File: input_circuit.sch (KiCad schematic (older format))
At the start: 10 parts, among them J2 IN, U3 MCP6004

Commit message: Layout complete
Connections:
- net OUT: now also U3.14; no longer U3.1
- net Vref: now also U3.13 (-); no longer U3.2 (-)
- net at C12.1, D4.2 (A), R5.2: now also U3.12 (+); no longer U3.3 (+)
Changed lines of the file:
@@
 AR Path="/5AD35DB7/5AD30D7B/5AD2255F" Ref="D33"  Part="1"
 AR Path="/5AD35DB7/5AD30D85/5AD2255F" Ref="D35"  Part="1"
-F 0 "D4" H 3200 2230 50  0000 L CNN
+F 0 "D18" H 3200 2230 50  0000 L CNN
 F 1 "4142" H 3100 2070 50  0000 L CNN
 F 2 "Diodes_SMD:D_MiniMELF_Standard" V 3250 2150 50  0001 C CNN
@@
 AR Path="/5AD35DB7/5AD30D7B/5AD22566" Ref="R46"  Part="1"
 AR Path="/5AD35DB7/5AD30D85/5AD22566" Ref="R49"  Part="1"
-F 0 "R4" H 2280 2370 50  0000 L CNN
+F 0 "R25" H 2280 2370 50  0000 L CNN
 F 1 "22k" H 2280 2310 50  0000 L CNN
 F 2 "Resistors_SMD:R_0603_HandSoldering" H 2250 2350 50  0001 C CNN
@@
 AR Path="/5AD35DB7/5AD30D7B/5AD2256D" Ref="C43"  Part="1"
 AR Path="/5AD35DB7/5AD30D85/5AD2256D" Ref="C45"  Part="1"
-F 0 "C12" H 3260 2620 50  0000 L CNN
+F 0 "C26" H 3260 2620 50  0000 L CNN
 F 1 "47n" H 3260 2470 50  0000 L CNN
 F 2 "Capacitors_SMD:C_0603_HandSoldering" H 3250 2550 50  0001 C CNN
@@
 AR Path="/5AD222D9/5AD22574" Ref="#PWR?"  Part="1"
 AR Path="/5AD2476B/5AD22574" Ref="#PWR?"  Part="1"
-AR Path="/5AD2F8CE/5AD30D3F/5AD22574" Ref="#PWR020"  Part="1"
-AR Path="/5AD2F8CE/5AD30D49/5AD22574" Ref="#PWR023"  Part="1"
-AR Path="/5AD2F8CE/5AD30D53/5AD22574" Ref="#PWR026"  Part="1"
-AR Path="/5AD2F8CE/5AD30D5D/5AD22574" Ref="#PWR029"  Part="1"
-AR Path="/5AD2F8CE/5AD30D67/5AD22574" Ref="#PWR032"  Part="1"
-AR Path="/5AD2F8CE/5AD30D71/5AD22574" Ref="#PWR035"  Part="1"
-AR Path="/5AD2F8CE/5AD30D7B/5AD22574" Ref="#PWR038"  Part="1"
-AR Path="/5AD2F8CE/5AD30D85/5AD22574" Ref="#PWR041"  Part="1"
+AR Path="/5AD2F8CE/5AD30D3F/5AD22574" Ref="#PWR24"  Part="1"
+AR Path="/5AD2F8CE/5AD30D49/5AD22574" Ref="#PWR27"  Part="1"
+AR Path="/5AD2F8CE/5AD30D53/5AD22574" Ref="#PWR30"  Part="1"
+AR Path="/5AD2F8CE/5AD30D5D/5AD22574" Ref="#PWR33"  Part="1"
+AR Path="/5AD2F8CE/5AD30D67/5AD22574" Ref="#PWR36"  Part="1"
+AR Path="/5AD2F8CE/5AD30D71/5AD22574" Ref="#PWR39"  Part="1"
+AR Path="/5AD2F8CE/5AD30D7B/5AD22574" Ref="#PWR42"  Part="1"
+AR Path="/5AD2F8CE/5AD30D85/5AD22574" Ref="#PWR45"  Part="1"
 AR Path="/5AD35DB7/5AD30D3F/5AD22574" Ref="#PWR049"  Part="1"
 AR Path="/5AD35DB7/5AD30D49/5AD22574" Ref="#PWR052"  Part="1"
@@
 AR Path="/5AD35DB7/5AD30D7B/5AD22574" Ref="#PWR067"  Part="1"
 AR Path="/5AD35DB7/5AD30D85/5AD22574" Ref="#PWR070"  Part="1"
-F 0 "#PWR020" H 3250 2600 50  0001 C CNN
+F 0 "#PWR45" H 3250 2600 50  0001 C CNN
 F 1 "GND" H 3250 2700 50  0000 C CNN
 F 2 "" H 3250 2850 50  0001 C CNN
@@
 AR Path="/5AD222D9/5AD2257A" Ref="#PWR?"  Part="1"
 AR Path="/5AD2476B/5AD2257A" Ref="#PWR?"  Part="1"
-AR Path="/5AD2F8CE/5AD30D3F/5AD2257A" Ref="#PWR021"  Part="1"
-AR Path="/5AD2F8CE/5AD30D49/5AD2257A" Ref="#PWR024"  Part="1"
-AR Path="/5AD2F8CE/5AD30D53/5AD2257A" Ref="#PWR027"  Part="1"
-AR Path="/5AD2F8CE/5AD30D5D/5AD2257A" Ref="#PWR030"  Part="1"
-AR Path="/5AD2F8CE/5AD30D67/5AD2257A" Ref="#PWR033"  Part="1"
-AR Path="/5AD2F8CE/5AD30D71/5AD2257A" Ref="#PWR036"  Part="1"
-AR Path="/5AD2F8CE/5AD30D7B/5AD2257A" Ref="#PWR039"  Part="1"
-AR Path="/5AD2F8CE/5AD30D85/5AD2257A" Ref="#PWR042"  Part="1"
+AR Path="/5AD2F8CE/5AD30D3F/5AD2257A" Ref="#PWR22"  Part="1"
+AR Path="/5AD2F8CE/5AD30D49/5AD2257A" Ref="#PWR25"  Part="1"
+AR Path="/5AD2F8CE/5AD30D53/5AD2257A" Ref="#PWR28"  Part="1"
+AR Path="/5AD2F8CE/5AD30D5D/5AD2257A" Ref="#PWR31"  Part="1"
+AR Path="/5AD2F8CE/5AD30D67/5AD2257A" Ref="#PWR34"  Part="1"
+AR Path="/5AD2F8CE/5AD30D71/5AD2257A" Ref="#PWR37"  Part="1"
+AR Path="/5AD2F8CE/5AD30D7B/5AD2257A" Ref="#PWR40"  Part="1"
+AR Path="/5AD2F8CE/5AD30D85/5AD2257A" Ref="#PWR43"  Part="1"
 AR Path="/5AD35DB7/5AD30D3F/5AD2257A" Ref="#PWR050"  Part="1"
 AR Path="/5AD35DB7/5AD30D49/5AD2257A" Ref="#PWR053"  Part="1"
@@
 AR Path="/5AD35DB7/5AD30D7B/5AD2257A" Ref="#PWR068"  Part="1"
 AR Path="/5AD35DB7/5AD30D85/5AD2257A" Ref="#PWR071"  Part="1"
-F 0 "#PWR021" H 3250 1800 50  0001 C CNN
+F 0 "#PWR43" H 3250 1800 50  0001 C CNN
 F 1 "VCOM" H 3250 2100 50  0000 C CNN
 F 2 "" H 3250 1950 50  0001 C CNN
@@
 AR Path="/5AD35DB7/5AD30D7B/5AD22A33" Ref="R48"  Part="1"
 AR Path="/5AD35DB7/5AD30D85/5AD22A33" Ref="R51"  Part="1"
-F 0 "R6" H 2830 2570 50  0000 L CNN
+F 0 "R27" H 2830 2570 50  0000 L CNN
 F 1 "4k7" H 2830 2510 50  0000 L CNN
 F 2 "Resistors_SMD:R_0603_HandSoldering" H 2800 2550 50  0001 C CNN
@@
 AR Path="/5AD35DB7/5AD30D7B/5AD22AD6" Ref="R47"  Part="1"
 AR Path="/5AD35DB7/5AD30D85/5AD22AD6" Ref="R50"  Part="1"
-F 0 "R5" H 3030 2370 50  0000 L CNN
+F 0 "R26" H 3030 2370 50  0000 L CNN
 F 1 "47k" H 3030 2310 50  0000 L CNN
 F 2 "Resistors_SMD:R_0603_HandSoldering" H 3000 2350 50  0001 C CNN
@@
 AR Path="/5AD35DB7/5AD30D7B/5AD234DB" Ref="J16"  Part="1"
 AR Path="/5AD35DB7/5AD30D85/5AD234DB" Ref="J17"  Part="1"
-F 0 "J2" H 1450 2700 50  0000 C TNN
+F 0 "J9" H 1450 2700 50  0000 C TNN
 F 1 "IN" V 1300 2450 50  0000 C TNN
 F 2 "Connectors_JST:JST_EH_B02B-EH-A_02x2.50mm_Straight" H 1450 2225 50  0001 C CNN
@@
 AR Path="/5AD35DB7/5AD30D7B/5AD23A10" Ref="D34"  Part="1"
 AR Path="/5AD35DB7/5AD30D85/5AD23A10" Ref="D36"  Part="1"
-F 0 "D5" H 2400 2630 50  0000 L CNN
+F 0 "D19" H 2400 2630 50  0000 L CNN
 F 1 "4142" H 2300 2470 50  0000 L CNN
 F 2 "Diodes_SMD:D_MiniMELF_Standard" V 2450 2550 50  0001 C CNN
@@
 $Comp
 L MCP6004 U?
-U 1 1 5AD26E51
+U 4 1 5AD26E51
 P 4100 2450
 AR Path="/5AD222D9/5AD26E51" Ref="U?"  Part="1"
@@
 AR Path="/5AD35DB7/5AD30D7B/5AD26E51" Ref="U7"  Part="3"
 AR Path="/5AD35DB7/5AD30D85/5AD26E51" Ref="U7"  Part="4"
-F 0 "U3" H 4100 2650 50  0000 L CNN
+F 0 "U4" H 4100 2650 50  0000 L CNN
 F 1 "MCP6004" H 4100 2250 50  0000 L CNN
 F 2 "Housings_SOIC:SOIC-14_3.9x8.7mm_Pitch1.27mm" H 4050 2550 50  0001 C CNN
 F 3 "" H 4150 2650 50  0001 C CNN
-	1    4100 2450
+	4    4100 2450
 	1    0    0    -1
 $EndComp
@@
 P 4000 1950
 AR Path="/5AD222D9/5AD26F10" Ref="#PWR?"  Part="1"
-AR Path="/5AD2F8CE/5AD30D3F/5AD26F10" Ref="#PWR022"  Part="1"
-AR Path="/5AD2F8CE/5AD30D49/5AD26F10" Ref="#PWR025"  Part="1"
-AR Path="/5AD2F8CE/5AD30D53/5AD26F10" Ref="#PWR028"  Part="1"
-AR Path="/5AD2F8CE/5AD30D5D/5AD26F10" Ref="#PWR031"  Part="1"
-AR Path="/5AD2F8CE/5AD30D67/5AD26F10" Ref="#PWR034"  Part="1"
-AR Path="/5AD2F8CE/5AD30D71/5AD26F10" Ref="#PWR037"  Part="1"
-AR Path="/5AD2F8CE/5AD30D7B/5AD26F10" Ref="#PWR040"  Part="1"
-AR Path="/5AD2F8CE/5AD30D85/5AD26F10" Ref="#PWR043"  Part="1"
+AR Path="/5AD2F8CE/5AD30D3F/5AD26F10" Ref="#PWR23"  Part="1"
+AR Path="/5AD2F8CE/5AD30D49/5AD26F10" Ref="#PWR26"  Part="1"
+AR Path="/5AD2F8CE/5AD30D53/5AD26F10" Ref="#PWR29"  Part="1"
+AR Path="/5AD2F8CE/5AD30D5D/5AD26F10" Ref="#PWR32"  Part="1"
+AR Path="/5AD2F8CE/5AD30D67/5AD26F10" Ref="#PWR35"  Part="1"
+AR Path="/5AD2F8CE/5AD30D71/5AD26F10" Ref="#PWR38"  Part="1"
+AR Path="/5AD2F8CE/5AD30D7B/5AD26F10" Ref="#PWR41"  Part="1"
+AR Path="/5AD2F8CE/5AD30D85/5AD26F10" Ref="#PWR44"  Part="1"
 AR Path="/5AD35DB7/5AD30D3F/5AD26F10" Ref="#PWR051"  Part="1"
 AR Path="/5AD35DB7/5AD30D49/5AD26F10" Ref="#PWR054"  Part="1"
@@
 AR Path="/5AD35DB7/5AD30D7B/5AD26F10" Ref="#PWR069"  Part="1"
 AR Path="/5AD35DB7/5AD30D85/5AD26F10" Ref="#PWR072"  Part="1"
-F 0 "#PWR022" H 4000 1800 50  0001 C CNN
+F 0 "#PWR44" H 4000 1800 50  0001 C CNN
 F 1 "VDD" H 4000 2100 50  0000 C CNN
 F 2 "" H 4000 1950 50  0001 C CNN
@@
 AR Path="/5AD35DB7/5AD30D7B/5AD5B9C3" Ref="C42"  Part="1"
 AR Path="/5AD35DB7/5AD30D85/5AD5B9C3" Ref="C44"  Part="1"
-F 0 "C11" H 1760 2520 50  0000 L CNN
+F 0 "C25" H 1760 2520 50  0000 L CNN
 F 1 "47n" H 1760 2370 50  0000 L CNN
 F 2 "Capacitors_SMD:C_0603_HandSoldering" H 1750 2450 50  0001 C CNN
@@
 AR Path="/5AD35DB7/5AD30D7B/5AD5BA8F" Ref="L16"  Part="1"
 AR Path="/5AD35DB7/5AD30D85/5AD5BA8F" Ref="L17"  Part="1"
-F 0 "L2" H 2025 2400 50  0000 L CNN
+F 0 "L9" H 2025 2400 50  0000 L CNN
 F 1 "Ferrite_Bead_Small" H 2025 2300 50  0001 L CNN
 F 2 "Resistors_SMD:R_0805_HandSoldering" V 1880 2350 50  0001 C CNN

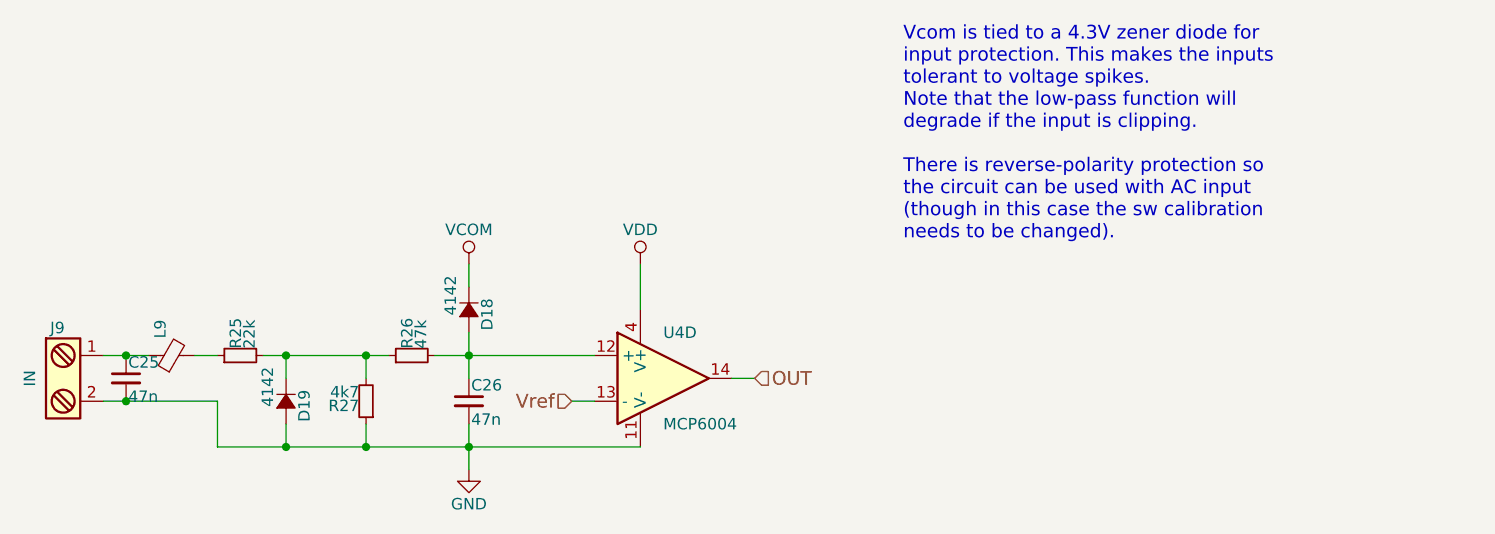
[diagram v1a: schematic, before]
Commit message: Add pullup option
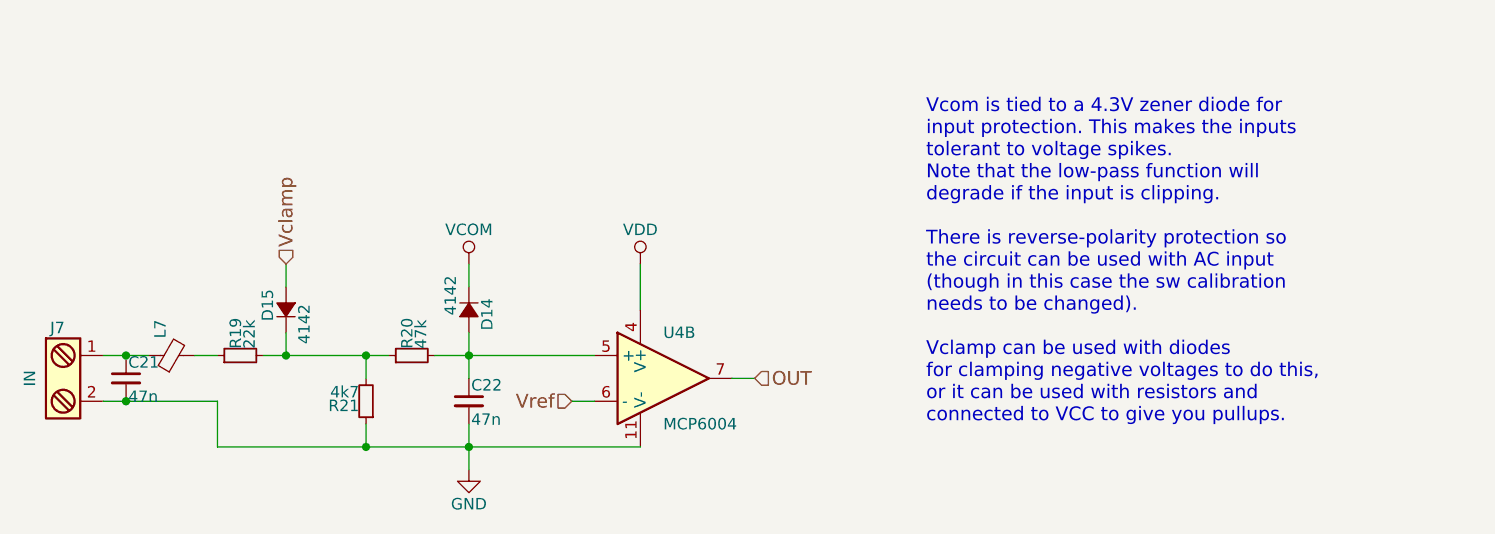
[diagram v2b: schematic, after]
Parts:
- D5: footprint Diodes_SMD:D_MiniMELF_Standard -> footprints:MiniMelf_0603_combo
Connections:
- net GND: no longer D5.2 (A)
- net OUT: now also U3.7; no longer U3.14
- net Vref: now also U3.6 (-); no longer U3.13 (-)
- net at C12.1, D4.2 (A), R5.2: now also U3.5 (+); no longer U3.12 (+)
- new net Vclamp: D5.2 (A)
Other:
- note added: "Vcom is tied to a 4.3V zener diode for\ninput protection. This makes the inputs\ntolerant to voltage spikes.\nNote that the low-pass function will\ndegrade if the input is clipping.\n\nThere is reverse-polarity protection so\nthe circuit can be used with AC input\n(though in this case the sw calibration\nneeds to be changed).\n\nVclamp can be used with diodes\nfor clamping negative voltages to do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"
- note removed: "Vcom is tied to a 4.3V zener diode for\ninput protection. This makes the inputs\ntolerant to voltage spikes.\nNote that the low-pass function will\ndegrade if the input is clipping.\n\nThere is reverse-polarity protection so\nthe circuit can be used with AC input\n(though in this case the sw calibration\nneeds to be changed)."
- moved on the sheet: D15
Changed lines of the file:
@@
 AR Path="/5AD35DB7/5AD30D7B/5AD2255F" Ref="D33"  Part="1"
 AR Path="/5AD35DB7/5AD30D85/5AD2255F" Ref="D35"  Part="1"
-F 0 "D18" H 3200 2230 50  0000 L CNN
+F 0 "D14" H 3200 2230 50  0000 L CNN
 F 1 "4142" H 3100 2070 50  0000 L CNN
 F 2 "Diodes_SMD:D_MiniMELF_Standard" V 3250 2150 50  0001 C CNN
@@
 AR Path="/5AD35DB7/5AD30D7B/5AD22566" Ref="R46"  Part="1"
 AR Path="/5AD35DB7/5AD30D85/5AD22566" Ref="R49"  Part="1"
-F 0 "R25" H 2280 2370 50  0000 L CNN
+F 0 "R19" H 2280 2370 50  0000 L CNN
 F 1 "22k" H 2280 2310 50  0000 L CNN
 F 2 "Resistors_SMD:R_0603_HandSoldering" H 2250 2350 50  0001 C CNN
@@
 AR Path="/5AD35DB7/5AD30D7B/5AD2256D" Ref="C43"  Part="1"
 AR Path="/5AD35DB7/5AD30D85/5AD2256D" Ref="C45"  Part="1"
-F 0 "C26" H 3260 2620 50  0000 L CNN
+F 0 "C22" H 3260 2620 50  0000 L CNN
 F 1 "47n" H 3260 2470 50  0000 L CNN
 F 2 "Capacitors_SMD:C_0603_HandSoldering" H 3250 2550 50  0001 C CNN
@@
 AR Path="/5AD222D9/5AD22574" Ref="#PWR?"  Part="1"
 AR Path="/5AD2476B/5AD22574" Ref="#PWR?"  Part="1"
-AR Path="/5AD2F8CE/5AD30D3F/5AD22574" Ref="#PWR24"  Part="1"
-AR Path="/5AD2F8CE/5AD30D49/5AD22574" Ref="#PWR27"  Part="1"
-AR Path="/5AD2F8CE/5AD30D53/5AD22574" Ref="#PWR30"  Part="1"
-AR Path="/5AD2F8CE/5AD30D5D/5AD22574" Ref="#PWR33"  Part="1"
-AR Path="/5AD2F8CE/5AD30D67/5AD22574" Ref="#PWR36"  Part="1"
-AR Path="/5AD2F8CE/5AD30D71/5AD22574" Ref="#PWR39"  Part="1"
-AR Path="/5AD2F8CE/5AD30D7B/5AD22574" Ref="#PWR42"  Part="1"
-AR Path="/5AD2F8CE/5AD30D85/5AD22574" Ref="#PWR45"  Part="1"
+AR Path="/5AD2F8CE/5AD30D3F/5AD22574" Ref="#PWR024"  Part="1"
+AR Path="/5AD2F8CE/5AD30D49/5AD22574" Ref="#PWR027"  Part="1"
+AR Path="/5AD2F8CE/5AD30D53/5AD22574" Ref="#PWR030"  Part="1"
+AR Path="/5AD2F8CE/5AD30D5D/5AD22574" Ref="#PWR033"  Part="1"
+AR Path="/5AD2F8CE/5AD30D67/5AD22574" Ref="#PWR036"  Part="1"
+AR Path="/5AD2F8CE/5AD30D71/5AD22574" Ref="#PWR039"  Part="1"
+AR Path="/5AD2F8CE/5AD30D7B/5AD22574" Ref="#PWR045"  Part="1"
+AR Path="/5AD2F8CE/5AD30D85/5AD22574" Ref="#PWR042"  Part="1"
 AR Path="/5AD35DB7/5AD30D3F/5AD22574" Ref="#PWR049"  Part="1"
 AR Path="/5AD35DB7/5AD30D49/5AD22574" Ref="#PWR052"  Part="1"
@@
 AR Path="/5AD35DB7/5AD30D7B/5AD22574" Ref="#PWR067"  Part="1"
 AR Path="/5AD35DB7/5AD30D85/5AD22574" Ref="#PWR070"  Part="1"
-F 0 "#PWR45" H 3250 2600 50  0001 C CNN
+F 0 "#PWR039" H 3250 2600 50  0001 C CNN
 F 1 "GND" H 3250 2700 50  0000 C CNN
 F 2 "" H 3250 2850 50  0001 C CNN
@@
 AR Path="/5AD222D9/5AD2257A" Ref="#PWR?"  Part="1"
 AR Path="/5AD2476B/5AD2257A" Ref="#PWR?"  Part="1"
-AR Path="/5AD2F8CE/5AD30D3F/5AD2257A" Ref="#PWR22"  Part="1"
-AR Path="/5AD2F8CE/5AD30D49/5AD2257A" Ref="#PWR25"  Part="1"
-AR Path="/5AD2F8CE/5AD30D53/5AD2257A" Ref="#PWR28"  Part="1"
-AR Path="/5AD2F8CE/5AD30D5D/5AD2257A" Ref="#PWR31"  Part="1"
-AR Path="/5AD2F8CE/5AD30D67/5AD2257A" Ref="#PWR34"  Part="1"
-AR Path="/5AD2F8CE/5AD30D71/5AD2257A" Ref="#PWR37"  Part="1"
-AR Path="/5AD2F8CE/5AD30D7B/5AD2257A" Ref="#PWR40"  Part="1"
-AR Path="/5AD2F8CE/5AD30D85/5AD2257A" Ref="#PWR43"  Part="1"
+AR Path="/5AD2F8CE/5AD30D3F/5AD2257A" Ref="#PWR025"  Part="1"
+AR Path="/5AD2F8CE/5AD30D49/5AD2257A" Ref="#PWR028"  Part="1"
+AR Path="/5AD2F8CE/5AD30D53/5AD2257A" Ref="#PWR031"  Part="1"
+AR Path="/5AD2F8CE/5AD30D5D/5AD2257A" Ref="#PWR034"  Part="1"
+AR Path="/5AD2F8CE/5AD30D67/5AD2257A" Ref="#PWR037"  Part="1"
+AR Path="/5AD2F8CE/5AD30D71/5AD2257A" Ref="#PWR040"  Part="1"
+AR Path="/5AD2F8CE/5AD30D7B/5AD2257A" Ref="#PWR046"  Part="1"
+AR Path="/5AD2F8CE/5AD30D85/5AD2257A" Ref="#PWR043"  Part="1"
 AR Path="/5AD35DB7/5AD30D3F/5AD2257A" Ref="#PWR050"  Part="1"
 AR Path="/5AD35DB7/5AD30D49/5AD2257A" Ref="#PWR053"  Part="1"
@@
 AR Path="/5AD35DB7/5AD30D7B/5AD2257A" Ref="#PWR068"  Part="1"
 AR Path="/5AD35DB7/5AD30D85/5AD2257A" Ref="#PWR071"  Part="1"
-F 0 "#PWR43" H 3250 1800 50  0001 C CNN
+F 0 "#PWR040" H 3250 1800 50  0001 C CNN
 F 1 "VCOM" H 3250 2100 50  0000 C CNN
 F 2 "" H 3250 1950 50  0001 C CNN
@@
 Wire Wire Line
 	3250 2050 3250 1950
-Text Notes 5150 1850 0    60   ~ 0
-Vcom is tied to a 4.3V zener diode for\ninput protection. This makes the inputs\ntolerant to voltage spikes.\nNote that the low-pass function will\ndegrade if the input is clipping.\n\nThere is reverse-polarity protection so\nthe circuit can be used with AC input\n(though in this case the sw calibration\nneeds to be changed).
+Text Notes 5250 2650 0    60   ~ 0
+Vcom is tied to a 4.3V zener diode for\ninput protection. This makes the inputs\ntolerant to voltage spikes.\nNote that the low-pass function will\ndegrade if the input is clipping.\n\nThere is reverse-polarity protection so\nthe circuit can be used with AC input\n(though in this case the sw calibration\nneeds to be changed).\n\nVclamp can be used with diodes\nfor clamping negative voltages to do this,\nor it can be used with resistors and\nconnected to VCC to give you pullups.
 $Comp
 L R_Small R?
@@
 AR Path="/5AD35DB7/5AD30D7B/5AD22A33" Ref="R48"  Part="1"
 AR Path="/5AD35DB7/5AD30D85/5AD22A33" Ref="R51"  Part="1"
-F 0 "R27" H 2830 2570 50  0000 L CNN
+F 0 "R21" H 2830 2570 50  0000 L CNN
 F 1 "4k7" H 2830 2510 50  0000 L CNN
 F 2 "Resistors_SMD:R_0603_HandSoldering" H 2800 2550 50  0001 C CNN
@@
 AR Path="/5AD35DB7/5AD30D7B/5AD22AD6" Ref="R47"  Part="1"
 AR Path="/5AD35DB7/5AD30D85/5AD22AD6" Ref="R50"  Part="1"
-F 0 "R26" H 3030 2370 50  0000 L CNN
+F 0 "R20" H 3030 2370 50  0000 L CNN
 F 1 "47k" H 3030 2310 50  0000 L CNN
 F 2 "Resistors_SMD:R_0603_HandSoldering" H 3000 2350 50  0001 C CNN
@@
 AR Path="/5AD35DB7/5AD30D7B/5AD234DB" Ref="J16"  Part="1"
 AR Path="/5AD35DB7/5AD30D85/5AD234DB" Ref="J17"  Part="1"
-F 0 "J9" H 1450 2700 50  0000 C TNN
+F 0 "J7" H 1450 2700 50  0000 C TNN
 F 1 "IN" V 1300 2450 50  0000 C TNN
 F 2 "Connectors_JST:JST_EH_B02B-EH-A_02x2.50mm_Straight" H 1450 2225 50  0001 C CNN
@@
 L D_Small_ALT D?
 U 1 1 5AD23A10
-P 2450 2550
+P 2450 2150
 AR Path="/5AD222D9/5AD23A10" Ref="D?"  Part="1"
 AR Path="/5AD2476B/5AD23A10" Ref="D?"  Part="1"
@@
 AR Path="/5AD35DB7/5AD30D7B/5AD23A10" Ref="D34"  Part="1"
 AR Path="/5AD35DB7/5AD30D85/5AD23A10" Ref="D36"  Part="1"
-F 0 "D19" H 2400 2630 50  0000 L CNN
-F 1 "4142" H 2300 2470 50  0000 L CNN
-F 2 "Diodes_SMD:D_MiniMELF_Standard" V 2450 2550 50  0001 C CNN
-F 3 "" V 2450 2550 50  0001 C CNN
-	1    2450 2550
-	0    1    1    0
+F 0 "D15" H 2400 2230 50  0000 L CNN
+F 1 "4142" H 2300 2070 50  0000 L CNN
+F 2 "footprints:MiniMelf_0603_combo" V 2450 2150 50  0001 C CNN
+F 3 "" V 2450 2150 50  0001 C CNN
+	1    2450 2150
+	0    -1   -1   0
 $EndComp
 Wire Wire Line
@@
 Connection ~ 3250 2750
 Connection ~ 2800 2750
-Wire Wire Line
-	2450 2750 2450 2650
-Connection ~ 2450 2750
-Wire Wire Line
-	2450 2450 2450 2350
 Connection ~ 2450 2350
 $Comp
 L MCP6004 U?
-U 4 1 5AD26E51
+U 2 1 5AD26E51
 P 4100 2450
 AR Path="/5AD222D9/5AD26E51" Ref="U?"  Part="1"
@@
 F 2 "Housings_SOIC:SOIC-14_3.9x8.7mm_Pitch1.27mm" H 4050 2550 50  0001 C CNN
 F 3 "" H 4150 2650 50  0001 C CNN
-	4    4100 2450
+	2    4100 2450
 	1    0    0    -1
 $EndComp
@@
 P 4000 1950
 AR Path="/5AD222D9/5AD26F10" Ref="#PWR?"  Part="1"
-AR Path="/5AD2F8CE/5AD30D3F/5AD26F10" Ref="#PWR23"  Part="1"
-AR Path="/5AD2F8CE/5AD30D49/5AD26F10" Ref="#PWR26"  Part="1"
-AR Path="/5AD2F8CE/5AD30D53/5AD26F10" Ref="#PWR29"  Part="1"
-AR Path="/5AD2F8CE/5AD30D5D/5AD26F10" Ref="#PWR32"  Part="1"
-AR Path="/5AD2F8CE/5AD30D67/5AD26F10" Ref="#PWR35"  Part="1"
-AR Path="/5AD2F8CE/5AD30D71/5AD26F10" Ref="#PWR38"  Part="1"
-AR Path="/5AD2F8CE/5AD30D7B/5AD26F10" Ref="#PWR41"  Part="1"
-AR Path="/5AD2F8CE/5AD30D85/5AD26F10" Ref="#PWR44"  Part="1"
+AR Path="/5AD2F8CE/5AD30D3F/5AD26F10" Ref="#PWR026"  Part="1"
+AR Path="/5AD2F8CE/5AD30D49/5AD26F10" Ref="#PWR029"  Part="1"
+AR Path="/5AD2F8CE/5AD30D53/5AD26F10" Ref="#PWR032"  Part="1"
+AR Path="/5AD2F8CE/5AD30D5D/5AD26F10" Ref="#PWR035"  Part="1"
+AR Path="/5AD2F8CE/5AD30D67/5AD26F10" Ref="#PWR038"  Part="1"
+AR Path="/5AD2F8CE/5AD30D71/5AD26F10" Ref="#PWR041"  Part="1"
+AR Path="/5AD2F8CE/5AD30D7B/5AD26F10" Ref="#PWR047"  Part="1"
+AR Path="/5AD2F8CE/5AD30D85/5AD26F10" Ref="#PWR044"  Part="1"
 AR Path="/5AD35DB7/5AD30D3F/5AD26F10" Ref="#PWR051"  Part="1"
 AR Path="/5AD35DB7/5AD30D49/5AD26F10" Ref="#PWR054"  Part="1"
@@
 AR Path="/5AD35DB7/5AD30D7B/5AD26F10" Ref="#PWR069"  Part="1"
 AR Path="/5AD35DB7/5AD30D85/5AD26F10" Ref="#PWR072"  Part="1"
-F 0 "#PWR44" H 4000 1800 50  0001 C CNN
+F 0 "#PWR041" H 4000 1800 50  0001 C CNN
 F 1 "VDD" H 4000 2100 50  0000 C CNN
 F 2 "" H 4000 1950 50  0001 C CNN
@@
 AR Path="/5AD35DB7/5AD30D7B/5AD5B9C3" Ref="C42"  Part="1"
 AR Path="/5AD35DB7/5AD30D85/5AD5B9C3" Ref="C44"  Part="1"
-F 0 "C25" H 1760 2520 50  0000 L CNN
+F 0 "C21" H 1760 2520 50  0000 L CNN
 F 1 "47n" H 1760 2370 50  0000 L CNN
 F 2 "Capacitors_SMD:C_0603_HandSoldering" H 1750 2450 50  0001 C CNN
@@
 AR Path="/5AD35DB7/5AD30D7B/5AD5BA8F" Ref="L16"  Part="1"
 AR Path="/5AD35DB7/5AD30D85/5AD5BA8F" Ref="L17"  Part="1"
-F 0 "L9" H 2025 2400 50  0000 L CNN
+F 0 "L7" H 2025 2400 50  0000 L CNN
 F 1 "Ferrite_Bead_Small" H 2025 2300 50  0001 L CNN
 F 2 "Resistors_SMD:R_0805_HandSoldering" V 1880 2350 50  0001 C CNN
@@
 Connection ~ 1750 2350
 Connection ~ 1750 2550
+Wire Wire Line
+	2450 2250 2450 2350
+Text HLabel 2450 1950 1    60   Input ~ 0
+Vclamp
+Wire Wire Line
+	2450 1950 2450 2050
 $EndSCHEMATC
